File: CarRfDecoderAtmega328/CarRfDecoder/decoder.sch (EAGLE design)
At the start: 48 parts, among them T1 BC847, T2 BC847, T3 IRLML6402, U2 RFM69CW, U3 MCP73831, U4 ATMEGA328P, U6 MIC5219 3.3V, Y1 16MHZ

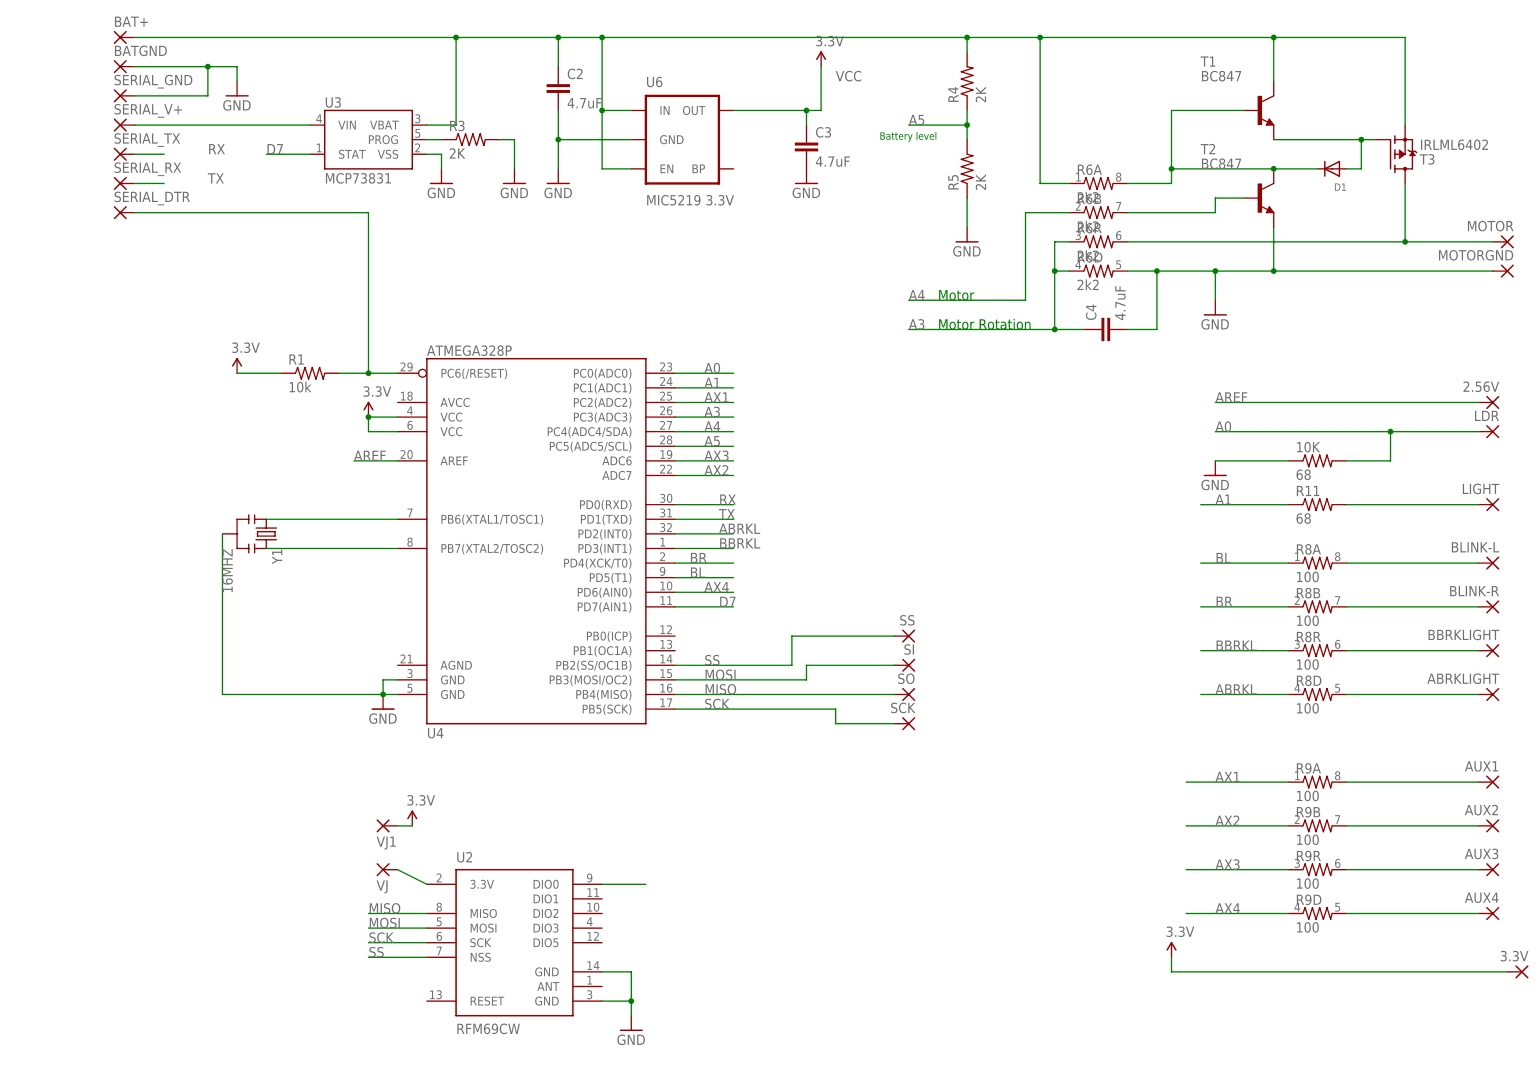
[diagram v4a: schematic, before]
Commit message: Add gnd pad. Reduce the size
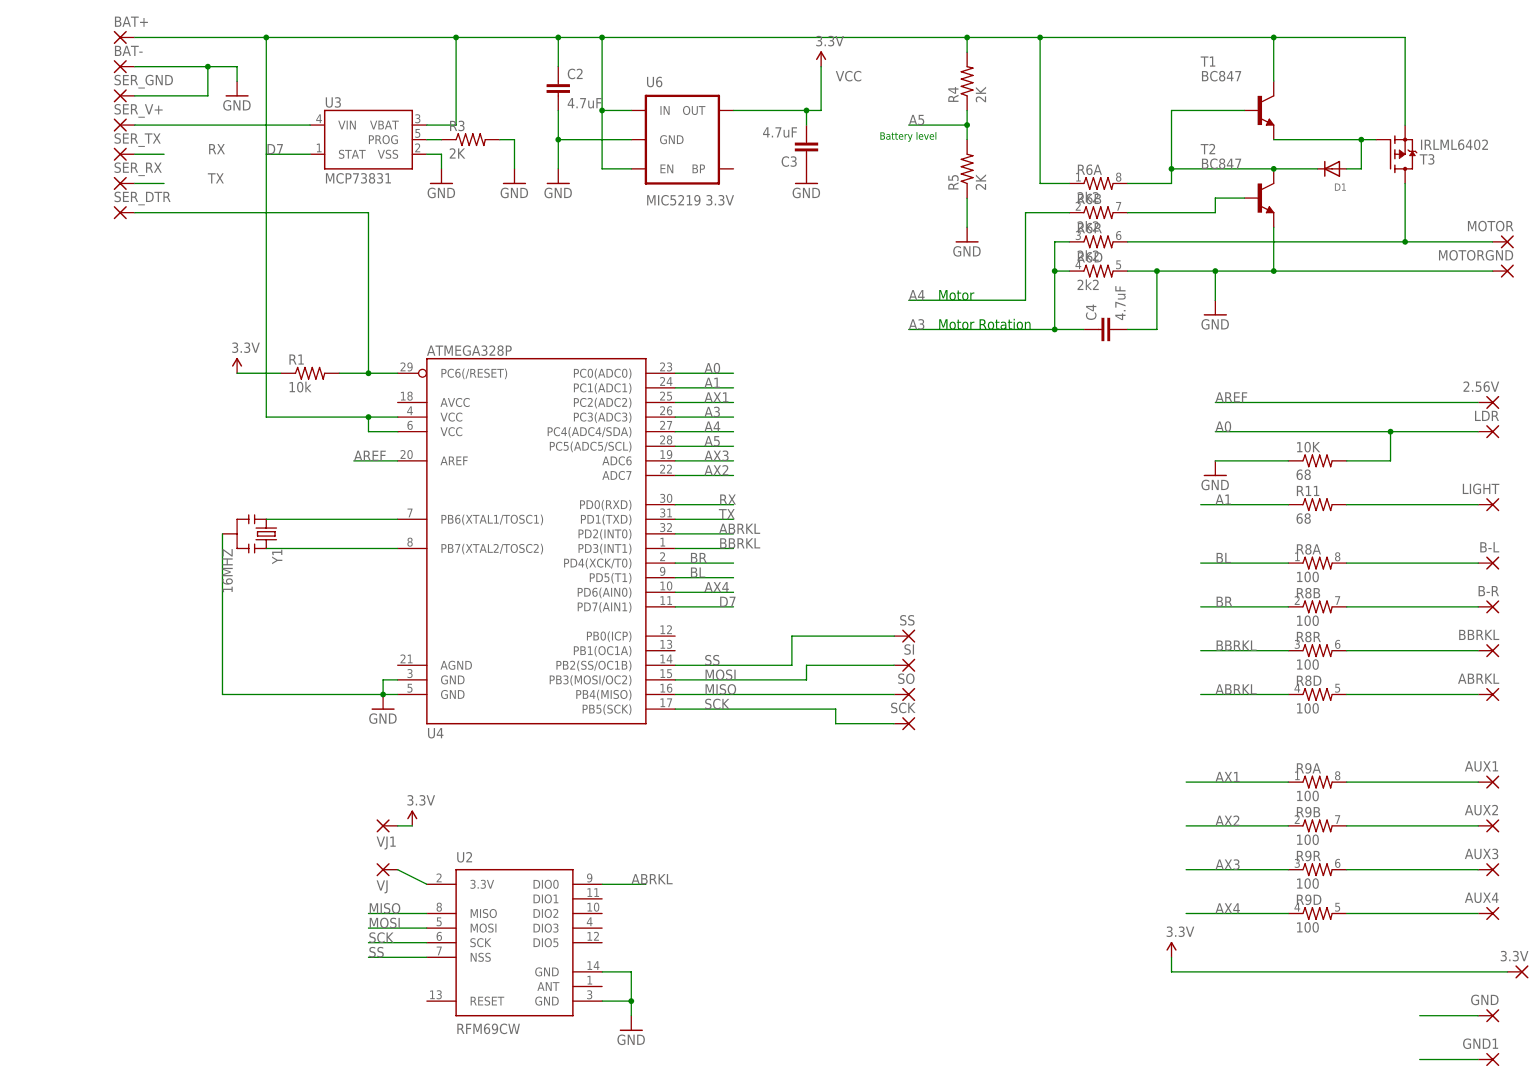
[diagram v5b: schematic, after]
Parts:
- added GND, GND1: (no value), wirepad:SMD2
- renumbered ABRKLIGHT to ABRKL, BATGND to BAT-, BBRKLIGHT to BBRKL, BLINK-L to B-L, BLINK-R to B-R, SERIAL_DTR to SER_DTR, SERIAL_GND to SER_GND, SERIAL_RX to SER_RX, SERIAL_TX to SER_TX, SERIAL_V+ to SER_V+
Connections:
- removed net N$10: BAT+.P, C2.1, R4.2, R6A.1, T1.C, T3.S, U3.VBAT, U6.EN, U6.IN
- new net BAT+: BAT+.P, C2.1, R4.2, R6A.1, T1.C, T3.S, U3.VBAT, U4.VCC@1, U4.VCC@2, U6.EN, U6.IN
- net GND: now also C3.1, GND.P, GND1.P; no longer C3.2
- net VCC: now also C3.2; no longer C3.1, U4.VCC@1, U4.VCC@2
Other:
- moved on the sheet: C3
